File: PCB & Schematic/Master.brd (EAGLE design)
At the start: 80 x 53.3 mm, 24 parts, among them M1 ARDUINO_R3_ICSP_NODIM, X1 MAB5SH, X2 MAB5SH

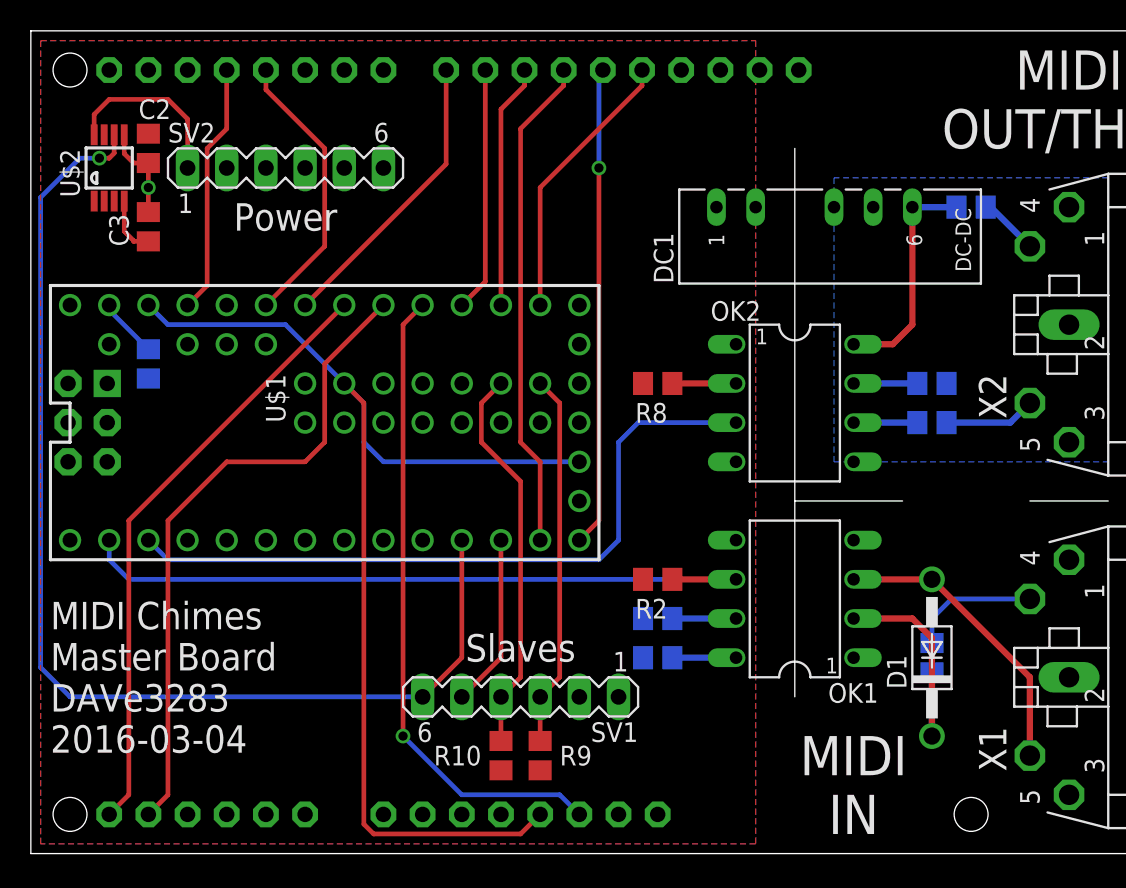
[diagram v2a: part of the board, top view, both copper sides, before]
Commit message: Power connector now 4 pin. Add doorbell notes.
The 6 pin connector was unnecessary, and risked confusion with the
slave board connector.

Added some notes on the cheap wireless doorbell I bought to
integrate with the chimes.
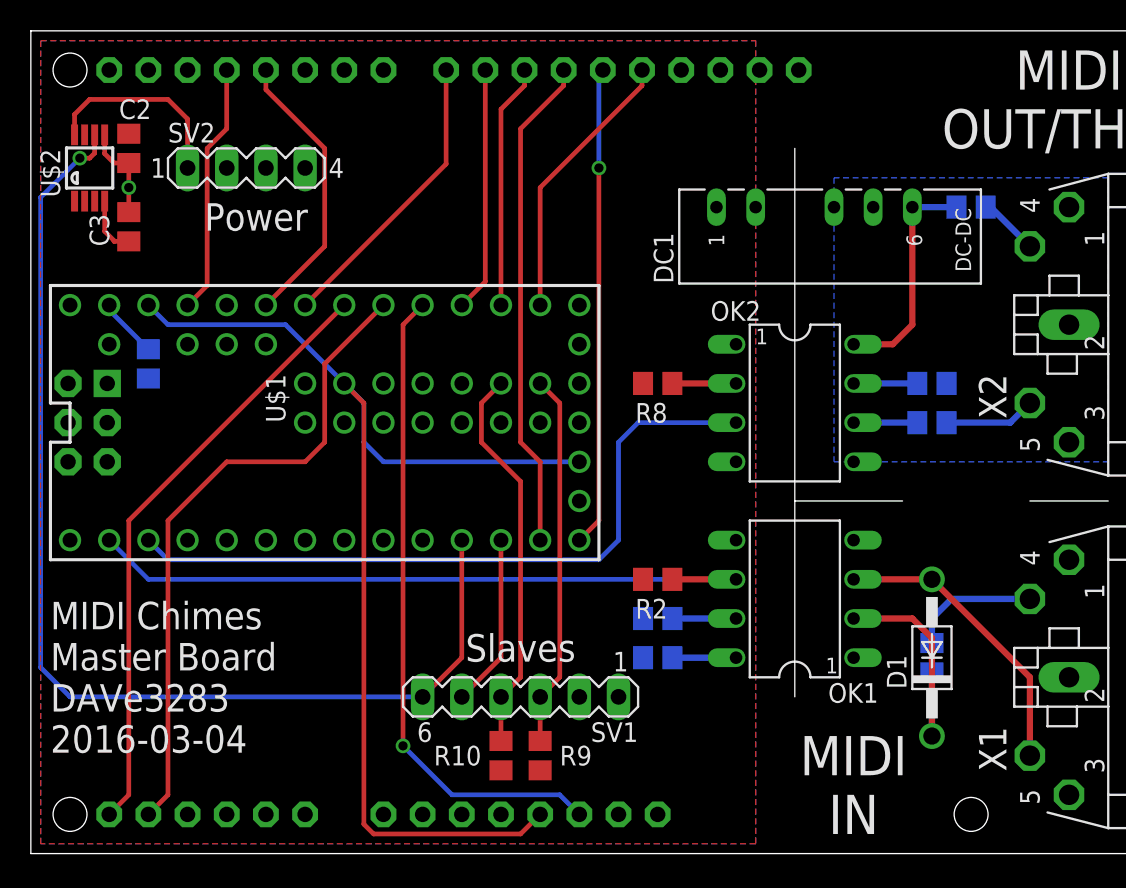
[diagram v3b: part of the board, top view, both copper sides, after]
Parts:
- C3: value 10n -> 0.01u
- SV2: device con-lstb:MA06-1 -> con-lstb:MA04-1
- moved SV2 2.54 mm to (14.0, 44.5)
- moved C2 1.27 mm to (6.35, 45.7)
- moved C3 1.27 mm to (6.35, 40.6)
- moved U$2 1.27 mm to (3.81, 44.5)
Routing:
- net PS_EN: track 74.4 -> 73.1 mm
- net N$11: track 11.5 -> 12.7 mm
- net MIDI_IN: track 46.6 -> 45.8 mm
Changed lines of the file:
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@@
 </polygon>
 <wire x1="49.53" y1="22.86" x2="56.515" y2="22.86" width="0" layer="20"/>
-<text x="16.51" y="41.275" size="1.778" layer="25" align="center">Power</text>
+<text x="14.605" y="41.275" size="1.778" layer="25" align="center">Power</text>
 <text x="31.75" y="13.335" size="1.778" layer="25" align="center">Slaves</text>
 <text x="1.27" y="11.43" size="1.778" layer="25" align="center-left">MIDI Chimes
@@
 <attribute name="OC_NEWARK" value="unknown" x="72.39" y="34.29" size="1.778" layer="27" rot="R90" display="off"/>
 </element>
-<element name="SV2" library="con-lstb" package="MA06-1" value="Power Supply" x="16.51" y="44.45" smashed="yes">
-<attribute name="OC_FARNELL" value="unknown" x="16.51" y="44.45" size="1.778" layer="27" display="off"/>
-<attribute name="MF" value="" x="16.51" y="44.45" size="1.778" layer="27" display="off"/>
-<attribute name="MPN" value="" x="16.51" y="44.45" size="1.778" layer="27" display="off"/>
-<attribute name="OC_NEWARK" value="unknown" x="16.51" y="44.45" size="1.778" layer="27" display="off"/>
-<attribute name="NAME" x="8.89" y="46.101" size="1.27" layer="25" ratio="10"/>
-</element>
-<element name="C2" library="resistor" package="C0805" value="0.1u" x="7.62" y="45.72" smashed="yes" rot="R270">
-<attribute name="NAME" x="6.985" y="47.625" size="1.27" layer="25"/>
-<attribute name="VALUE" x="9.525" y="47.625" size="1.27" layer="27"/>
-</element>
-<element name="C3" library="resistor" package="C0805" value="10n" x="7.62" y="40.64" rot="R90"/>
-<element name="U$2" library="DAVe3283" package="UMAX-U8-1" value="MAX16997" x="5.08" y="44.45" smashed="yes">
-<attribute name="MPN" value="MAX16997A" x="5.08" y="44.45" size="1.778" layer="27" display="off"/>
-<attribute name="NAME" x="3.175" y="42.545" size="1.27" layer="25" rot="R90"/>
+<element name="SV2" library="con-lstb" package="MA04-1" value="Power Supply" x="13.97" y="44.45">
+<attribute name="OC_FARNELL" value="unknown" x="13.97" y="44.45" size="1.778" layer="27" display="off"/>
+<attribute name="MF" value="" x="13.97" y="44.45" size="1.778" layer="27" display="off"/>
+<attribute name="MPN" value="" x="13.97" y="44.45" size="1.778" layer="27" display="off"/>
+<attribute name="OC_NEWARK" value="unknown" x="13.97" y="44.45" size="1.778" layer="27" display="off"/>
+</element>
+<element name="C2" library="resistor" package="C0805" value="0.1u" x="6.35" y="45.72" smashed="yes" rot="R270">
+<attribute name="NAME" x="5.715" y="47.625" size="1.27" layer="25"/>
+<attribute name="VALUE" x="8.255" y="47.625" size="1.27" layer="27"/>
+</element>
+<element name="C3" library="resistor" package="C0805" value="0.01u" x="6.35" y="40.64" rot="R90"/>
+<element name="U$2" library="DAVe3283" package="UMAX-U8-1" value="MAX16997" x="3.81" y="44.45" smashed="yes">
+<attribute name="MPN" value="MAX16997A" x="3.81" y="44.45" size="1.778" layer="27" display="off"/>
+<attribute name="NAME" x="1.905" y="42.545" size="1.27" layer="25" rot="R90"/>
 </element>
 </elements>
@@
 <contactref element="SV2" pad="4"/>
 <contactref element="U$2" pad="5"/>
-<via x="7.62" y="43.18" extent="1-16" drill="0.6" shape="square"/>
-<wire x1="6.055" y1="46.6" x2="6.055" y2="45.38" width="0.3048" layer="1"/>
-<wire x1="7.62" y1="44.77" x2="6.665" y2="44.77" width="0.3048" layer="1"/>
-<wire x1="6.665" y1="44.77" x2="6.055" y2="45.38" width="0.3048" layer="1"/>
-<wire x1="7.62" y1="43.18" x2="7.62" y2="44.77" width="0.3048" layer="1"/>
-<wire x1="7.62" y1="41.59" x2="7.62" y2="43.18" width="0.3048" layer="1"/>
+<via x="6.35" y="43.18" extent="1-16" drill="0.6" shape="square"/>
+<wire x1="4.785" y1="46.6" x2="4.785" y2="45.38" width="0.3048" layer="1"/>
+<wire x1="6.35" y1="44.77" x2="5.395" y2="44.77" width="0.3048" layer="1"/>
+<wire x1="5.395" y1="44.77" x2="4.785" y2="45.38" width="0.3048" layer="1"/>
+<wire x1="6.35" y1="43.18" x2="6.35" y2="44.77" width="0.3048" layer="1"/>
+<wire x1="6.35" y1="41.59" x2="6.35" y2="43.18" width="0.3048" layer="1"/>
 </signal>
 <signal name="VIN">
@@
 <contactref element="SV1" pad="6"/>
 <contactref element="U$1" pad="9"/>
-<wire x1="5.405" y1="45.41" x2="5.08" y2="45.085" width="0.3048" layer="1"/>
-<wire x1="5.08" y1="45.085" x2="4.445" y2="45.085" width="0.3048" layer="1"/>
-<via x="4.445" y="45.085" extent="1-16" drill="0.6" shape="square"/>
-<wire x1="4.445" y1="45.085" x2="3.175" y2="45.085" width="0.3048" layer="16"/>
-<wire x1="3.175" y1="45.085" x2="0.635" y2="42.545" width="0.3048" layer="16"/>
+<wire x1="4.135" y1="45.41" x2="3.81" y2="45.085" width="0.3048" layer="1"/>
+<wire x1="3.81" y1="45.085" x2="3.175" y2="45.085" width="0.3048" layer="1"/>
+<via x="3.175" y="45.085" extent="1-16" drill="0.6" shape="square"/>
 <wire x1="2.54" y1="10.16" x2="25.4" y2="10.16" width="0.3048" layer="16"/>
 <wire x1="27.94" y1="20.32" x2="27.94" y2="12.7" width="0.3048" layer="1"/>
 <wire x1="27.94" y1="12.7" x2="25.4" y2="10.16" width="0.3048" layer="1"/>
-<wire x1="0.635" y1="42.545" x2="0.635" y2="12.065" width="0.3048" layer="16"/>
 <wire x1="0.635" y1="12.065" x2="2.54" y2="10.16" width="0.3048" layer="16"/>
 <contactref element="U$2" pad="6"/>
-<wire x1="5.405" y1="46.6" x2="5.405" y2="45.41" width="0.3048" layer="1"/>
+<wire x1="4.135" y1="46.6" x2="4.135" y2="45.41" width="0.3048" layer="1"/>
+<wire x1="3.175" y1="45.085" x2="0.635" y2="42.545" width="0.3048" layer="16"/>
+<wire x1="0.635" y1="42.545" x2="0.635" y2="12.065" width="0.3048" layer="16"/>
 </signal>
 <signal name="ADDR_LATCH">
@@
 <contactref element="M1" pad="RESET"/>
 <contactref element="U$1" pad="17/A3"/>
+<via x="24.13" y="6.985" extent="1-16" drill="0.6" shape="square"/>
+<wire x1="25.4" y1="35.56" x2="24.13" y2="34.29" width="0.3048" layer="1"/>
+<wire x1="24.13" y1="34.29" x2="24.13" y2="6.985" width="0.3048" layer="1"/>
 <wire x1="35.56" y1="2.54" x2="34.29" y2="3.81" width="0.3048" layer="16"/>
-<wire x1="34.29" y1="3.81" x2="27.94" y2="3.81" width="0.3048" layer="16"/>
-<wire x1="27.94" y1="3.81" x2="24.13" y2="7.62" width="0.3048" layer="16"/>
-<via x="24.13" y="7.62" extent="1-16" drill="0.6" shape="square"/>
-<wire x1="25.4" y1="35.56" x2="24.13" y2="34.29" width="0.3048" layer="1"/>
-<wire x1="24.13" y1="34.29" x2="24.13" y2="7.62" width="0.3048" layer="1"/>
+<wire x1="34.29" y1="3.81" x2="27.305" y2="3.81" width="0.3048" layer="16"/>
+<wire x1="27.305" y1="3.81" x2="24.13" y2="6.985" width="0.3048" layer="16"/>
 </signal>
 <signal name="TOUCH_CS">
@@
 <contactref element="U$1" pad="0"/>
 <wire x1="41.59" y1="17.78" x2="45.72" y2="17.78" width="0.4064" layer="1"/>
-<wire x1="5.08" y1="20.32" x2="5.08" y2="19.05" width="0.3048" layer="16"/>
-<wire x1="5.08" y1="19.05" x2="6.35" y2="17.78" width="0.3048" layer="16"/>
-<wire x1="6.35" y1="17.78" x2="45.72" y2="17.78" width="0.3048" layer="16"/>
+<wire x1="5.08" y1="20.32" x2="7.62" y2="17.78" width="0.3048" layer="16"/>
+<wire x1="7.62" y1="17.78" x2="45.72" y2="17.78" width="0.3048" layer="16"/>
 </signal>
 <signal name="N$2">
@@
 <contactref element="X1" pad="4"/>
 <contactref element="R4" pad="2"/>
-<wire x1="64.77" y1="16.51" x2="59.69" y2="16.51" width="0.3048" layer="16"/>
-<wire x1="59.69" y1="16.51" x2="58.42" y2="15.24" width="0.3048" layer="16"/>
-<wire x1="58.42" y1="15.24" x2="58.42" y2="13.65" width="0.3048" layer="16"/>
+<wire x1="64.77" y1="16.51" x2="59.69" y2="16.51" width="0.4064" layer="16"/>
+<wire x1="59.69" y1="16.51" x2="58.42" y2="15.24" width="0.4064" layer="16"/>
+<wire x1="58.42" y1="15.24" x2="58.42" y2="13.65" width="0.4064" layer="16"/>
 </signal>
 <signal name="N$3">
@@
 <contactref element="SV2" pad="1"/>
 <contactref element="U$2" pad="8"/>
-<wire x1="4.105" y1="46.6" x2="4.105" y2="47.92" width="0.3048" layer="1"/>
-<wire x1="4.105" y1="47.92" x2="5.08" y2="48.895" width="0.3048" layer="1"/>
-<wire x1="5.08" y1="48.895" x2="8.89" y2="48.895" width="0.3048" layer="1"/>
+<wire x1="2.835" y1="46.6" x2="2.835" y2="47.92" width="0.3048" layer="1"/>
+<wire x1="2.835" y1="47.92" x2="3.81" y2="48.895" width="0.3048" layer="1"/>
+<wire x1="3.81" y1="48.895" x2="8.89" y2="48.895" width="0.3048" layer="1"/>
 <wire x1="8.89" y1="48.895" x2="10.16" y2="47.625" width="0.3048" layer="1"/>
 <wire x1="10.16" y1="47.625" x2="10.16" y2="44.45" width="0.3048" layer="1"/>
@@
 <contactref element="U$2" pad="4"/>
 <contactref element="C3" pad="1"/>
-<wire x1="6.055" y1="42.3" x2="6.055" y2="40.345" width="0.3048" layer="1"/>
-<wire x1="7.62" y1="39.69" x2="6.665" y2="39.69" width="0.3048" layer="1"/>
-<wire x1="6.665" y1="39.69" x2="6.665" y2="39.735" width="0.3048" layer="1"/>
-<wire x1="6.665" y1="39.735" x2="6.055" y2="40.345" width="0.3048" layer="1"/>
+<wire x1="4.785" y1="42.3" x2="4.785" y2="40.345" width="0.3048" layer="1"/>
+<wire x1="6.35" y1="39.69" x2="5.395" y2="39.69" width="0.3048" layer="1"/>
+<wire x1="5.395" y1="39.69" x2="5.395" y2="39.735" width="0.3048" layer="1"/>
+<wire x1="5.395" y1="39.735" x2="4.785" y2="40.345" width="0.3048" layer="1"/>
 </signal>
 </signals>

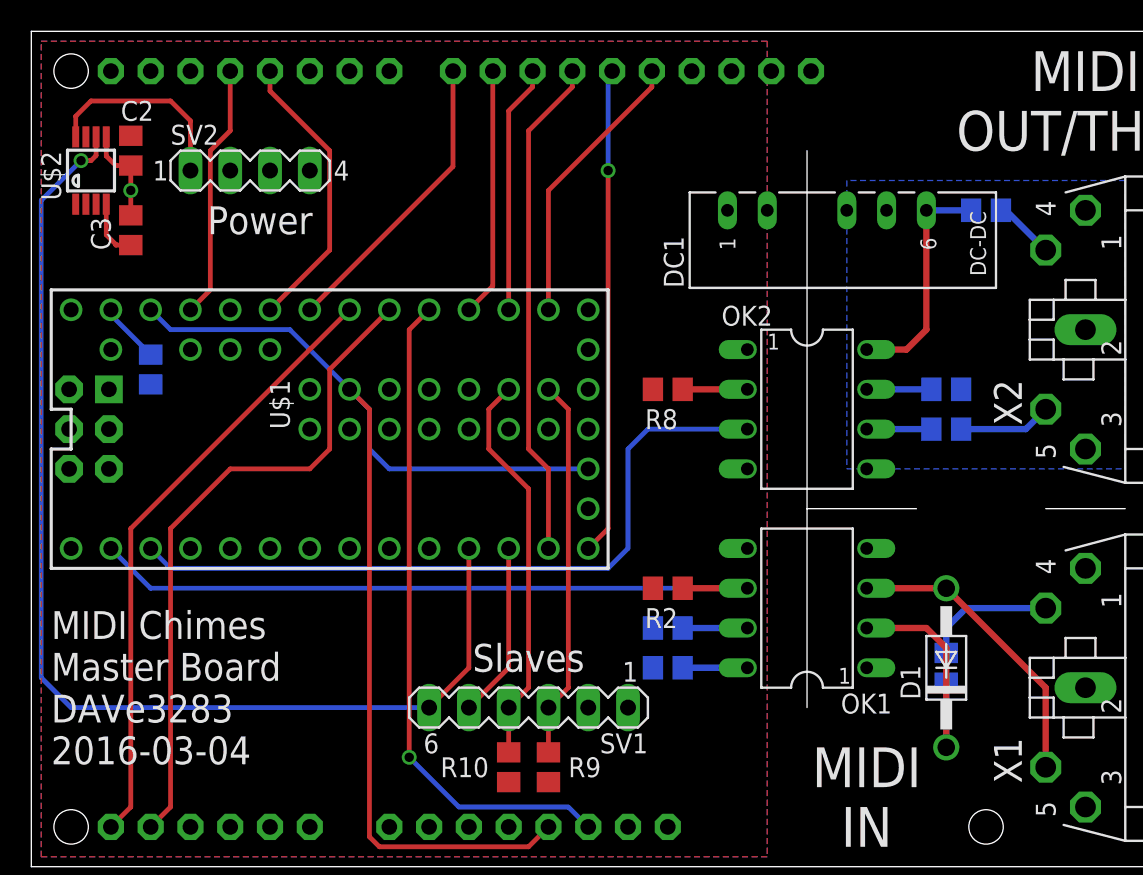
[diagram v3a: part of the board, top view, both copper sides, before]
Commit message: Add connector for wireless doorbell.
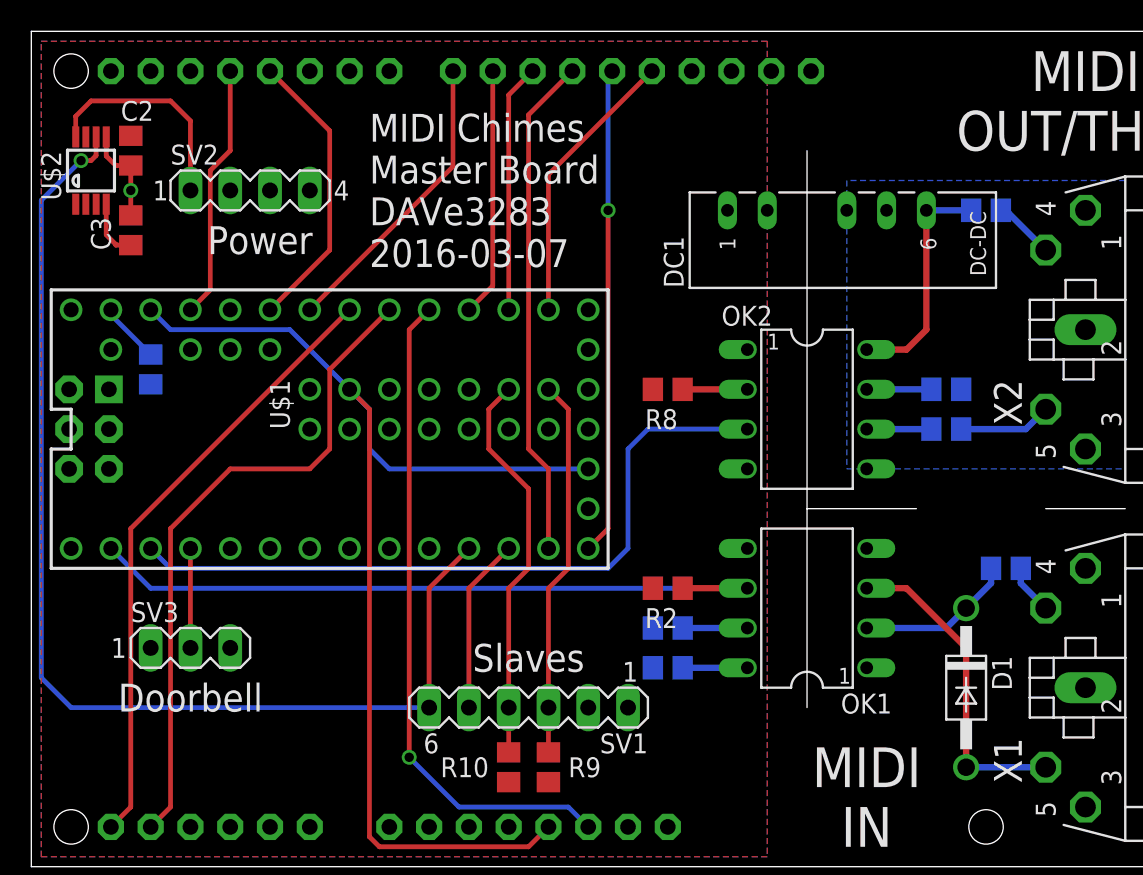
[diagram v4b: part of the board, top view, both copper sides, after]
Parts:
- added SV3: Doorbell, con-lstb:MA03-1
- moved R4 7.41 mm to (62.2, 19.1), turned to 180 degrees
- moved D1 1.80 mm to (59.7, 11.4), turned to 270 degrees
- moved SV2 1.27 mm to (14.0, 43.2)
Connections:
- new net DOORBELL_IN: SV3.2, U$1.2
- net +5V: now also SV3.3
- net GND: now also SV3.1
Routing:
- net DOORBELL_IN: track 0.00 -> 6.35 mm
- net N$3: track 16.1 -> 10.1 mm
- net N$4: track 8.47 -> 3.20 mm
- net N$5: track 19.1 -> 20.6 mm
- net N$11: track 12.7 -> 14.0 mm
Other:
- board text added: "Doorbell"
- board text added: "MIDI Chimes Master Board DAVe3283 2016-03-07"
- board text removed: "MIDI Chimes Master Board DAVe3283 2016-03-04"
